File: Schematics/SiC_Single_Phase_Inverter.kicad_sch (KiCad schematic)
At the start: 4 parts, among them J1 23AH8786-Red, J2 23AH8785-Black, J3 23AH8786-Red, J4 23AH8785-Black

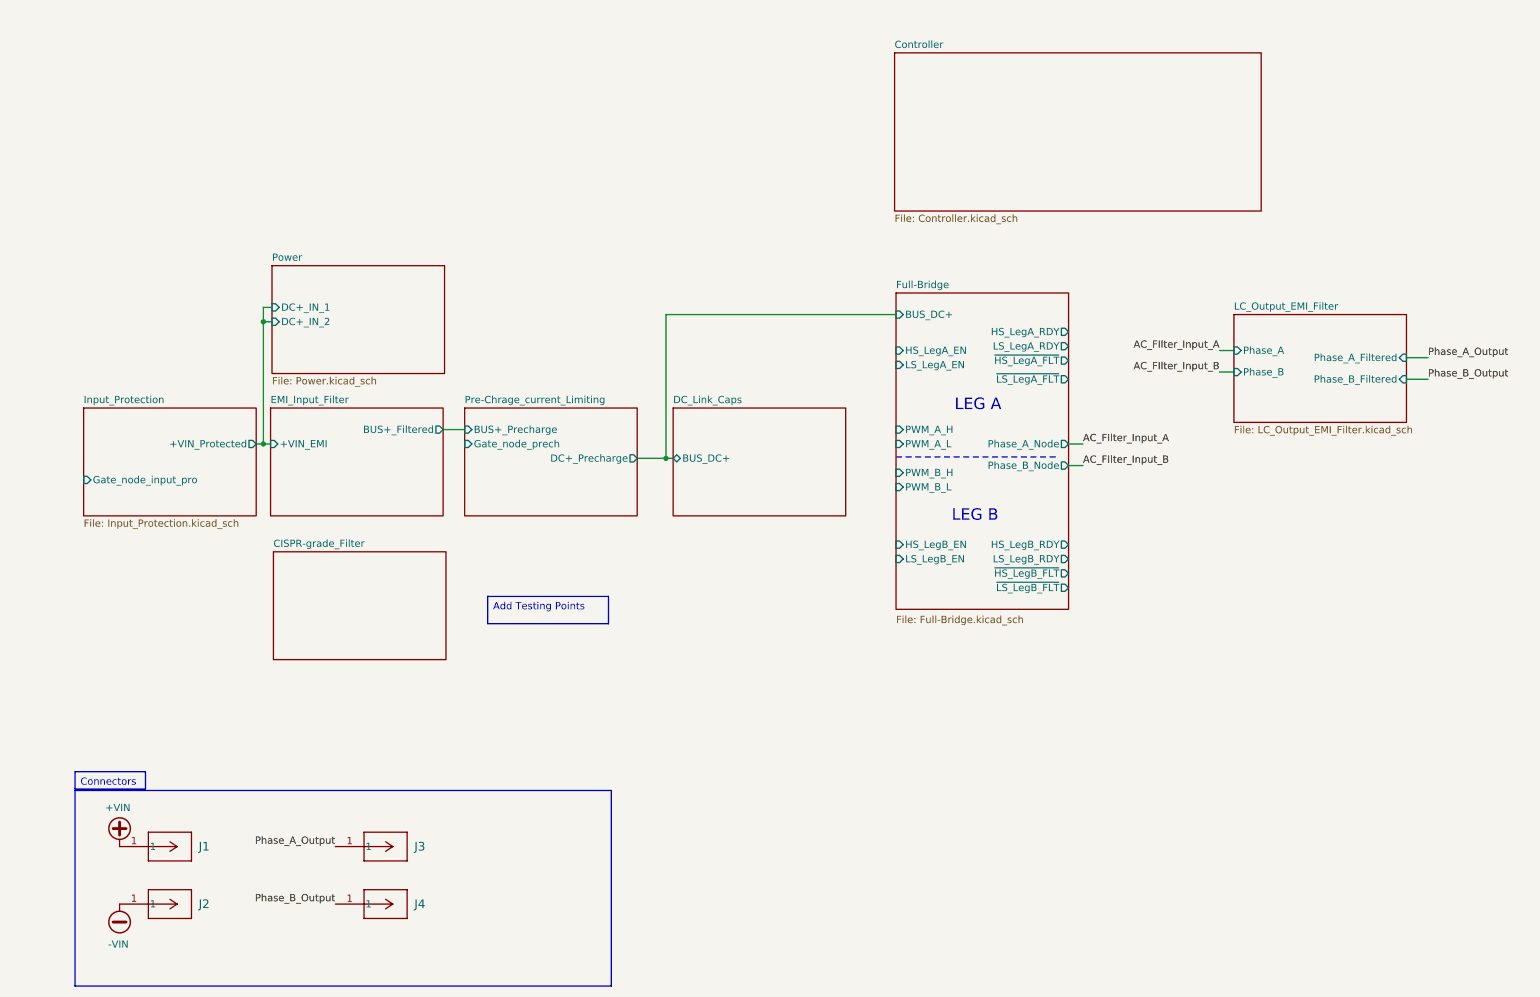
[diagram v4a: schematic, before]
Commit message: WIP: Work on Controller layout, and fixed some sheet text and positions
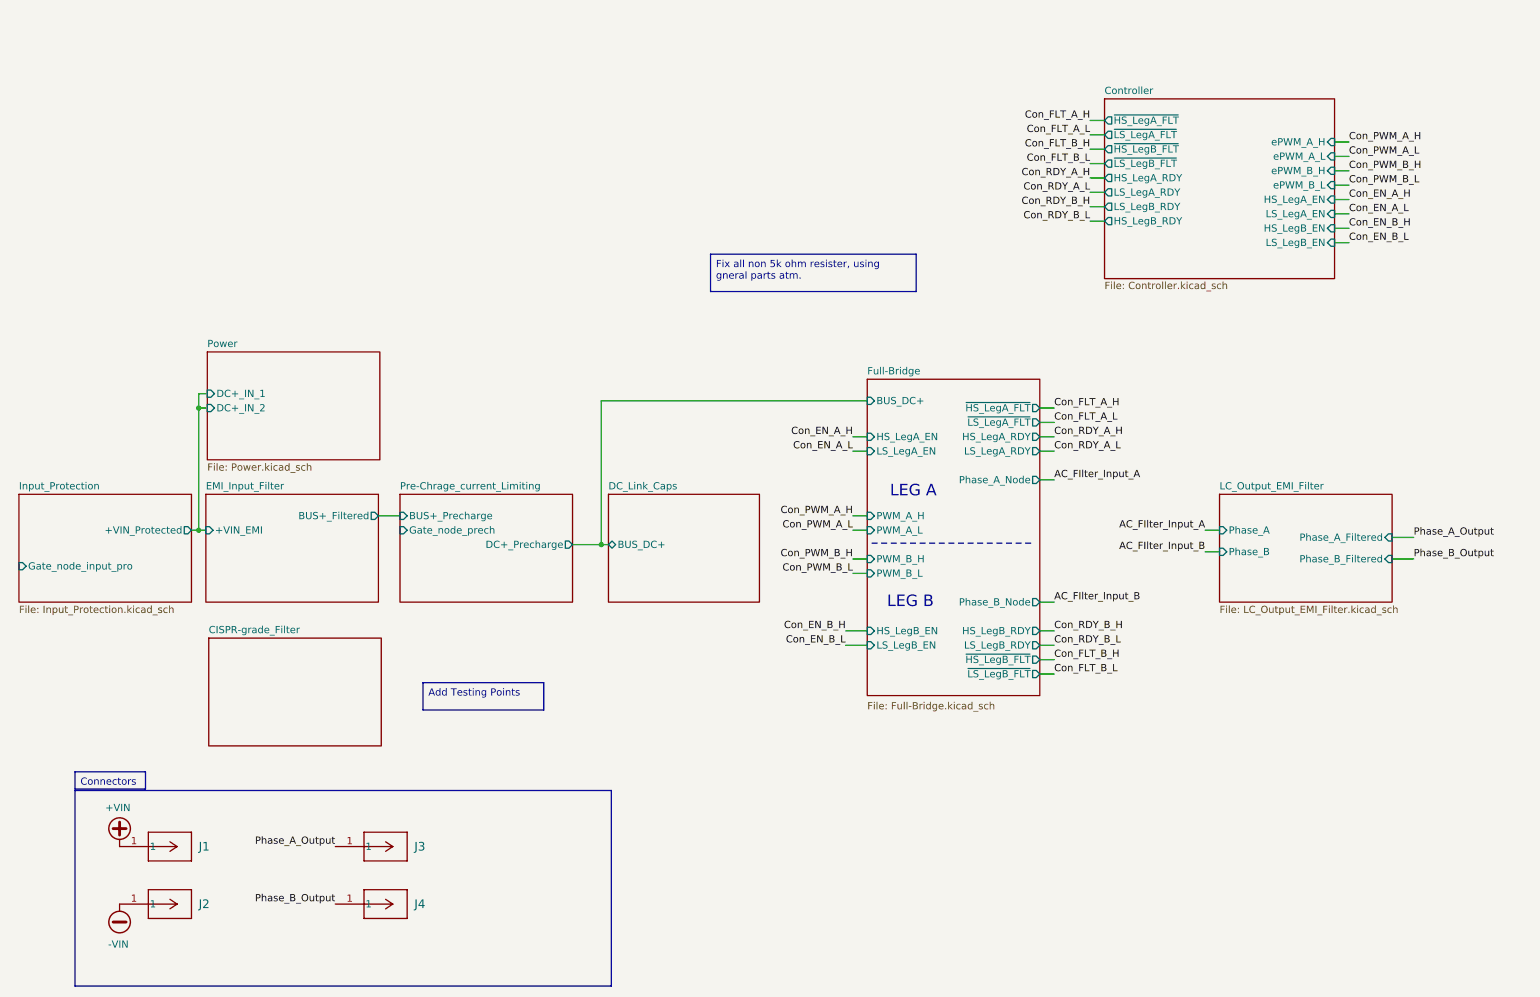
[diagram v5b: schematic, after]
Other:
- sheet Controller ports: added HS_LegA_EN, HS_LegA_RDY, HS_LegB_EN, HS_LegB_RDY, LS_LegA_EN, LS_LegA_RDY, LS_LegB_EN, LS_LegB_RDY, ePWM_A_H, ePWM_A_L, ePWM_B_H, ePWM_B_L, ~{HS_LegA_FLT}, ~{HS_LegB_FLT}, ~{LS_LegA_FLT}, ~{LS_LegB_FLT}; removed none

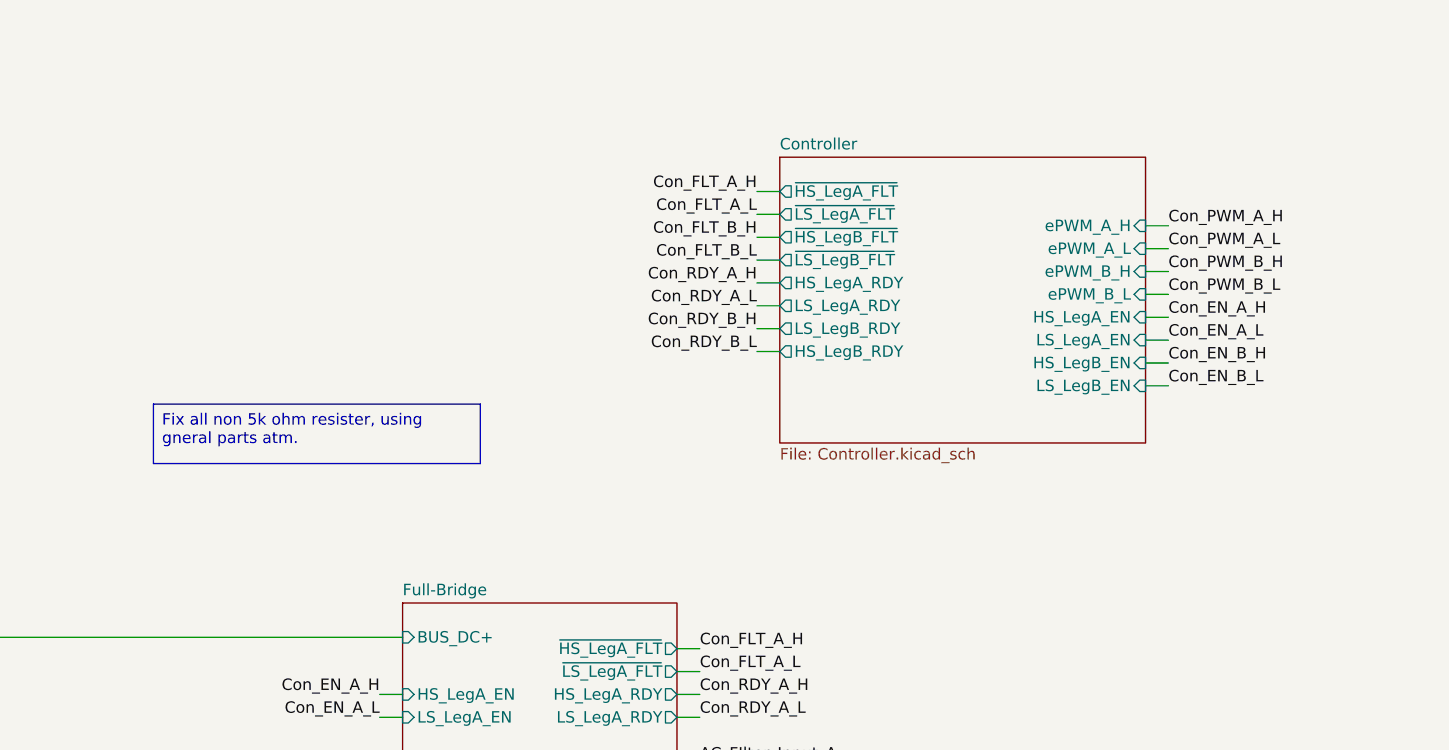
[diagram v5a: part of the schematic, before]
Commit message: [WIP Controller Subsheet]
- Added USB sub sheet to allow use of a USB connection to controller
- Added USB parts for USB Circuit
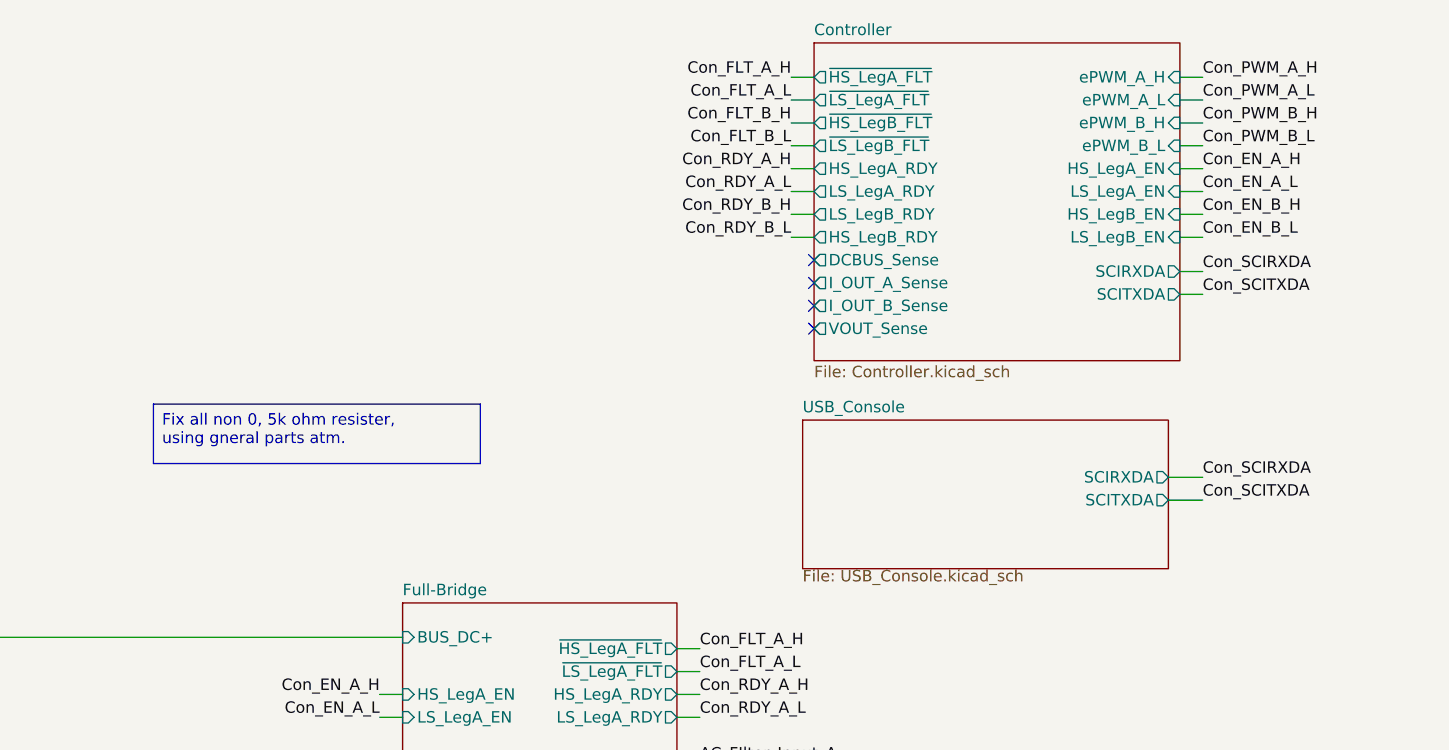
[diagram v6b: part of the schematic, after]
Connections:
- no-connect marks 0 -> 4
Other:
- added sheet USB_Console (USB_Console.kicad_sch)
- sheet Controller ports: added DCBUS_Sense, I_OUT_A_Sense, I_OUT_B_Sense, SCIRXDA, SCITXDA, VOUT_Sense; removed none

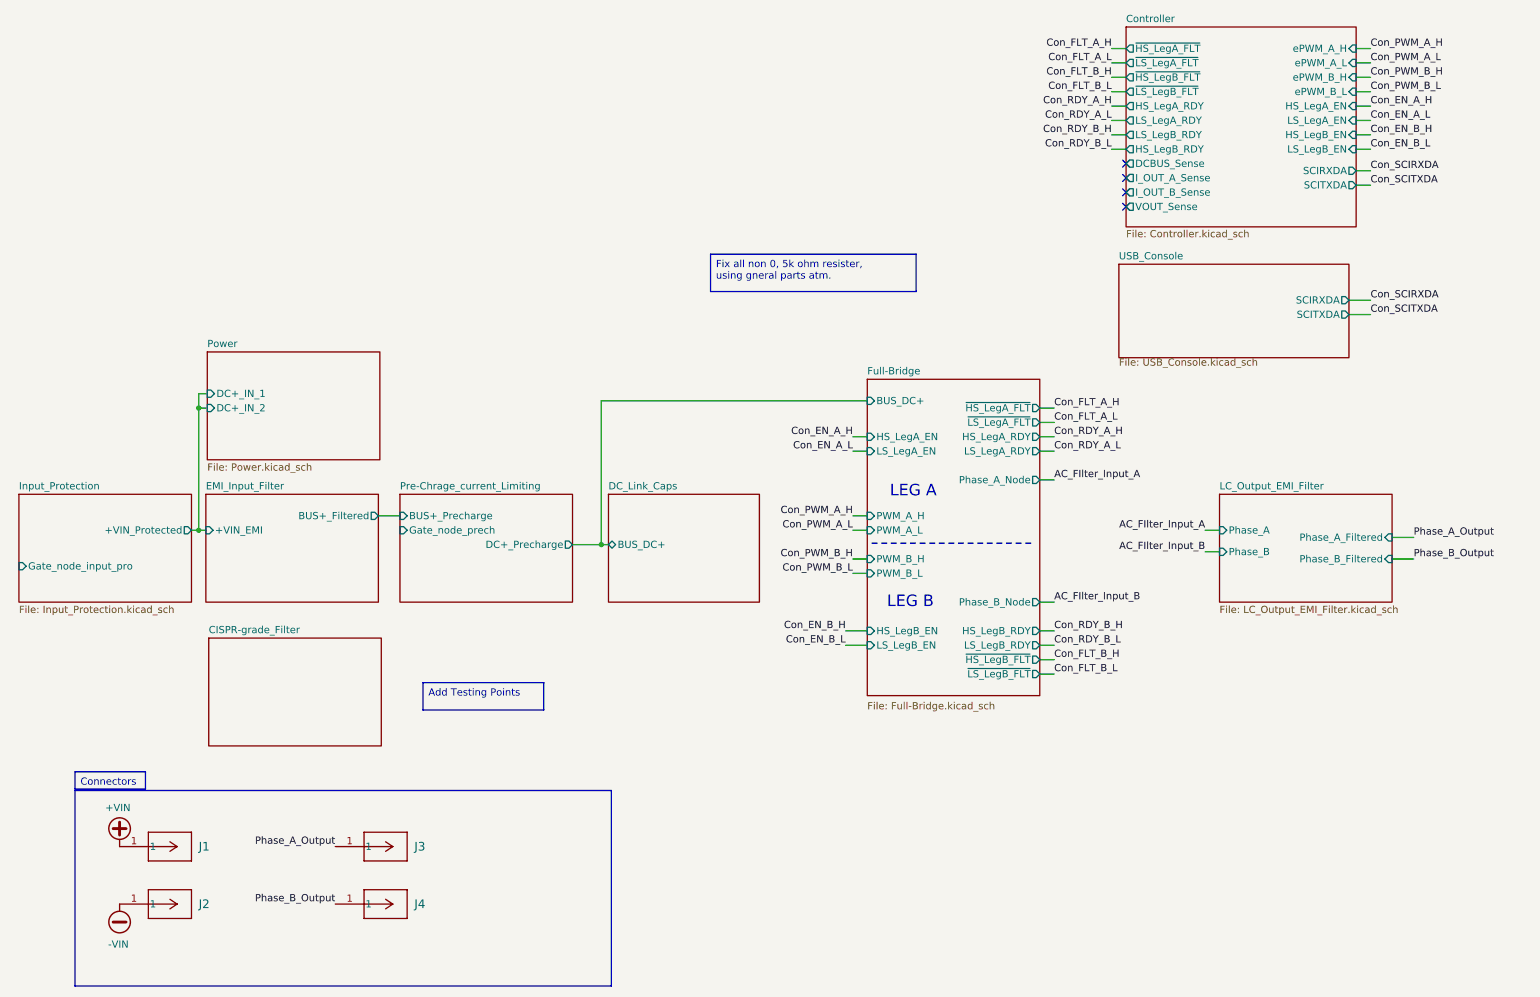
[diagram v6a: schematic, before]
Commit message: [Milestone Compelted Controller and USB]
- Added Test Points
- Completed USB circuit to Controller
- Wired up Controller
- Added Connectors to Power Subsheet and 12pin from cotnroller to Full
  Bridge
- Added 3d models for USB compoents
- General fixes to subsheets
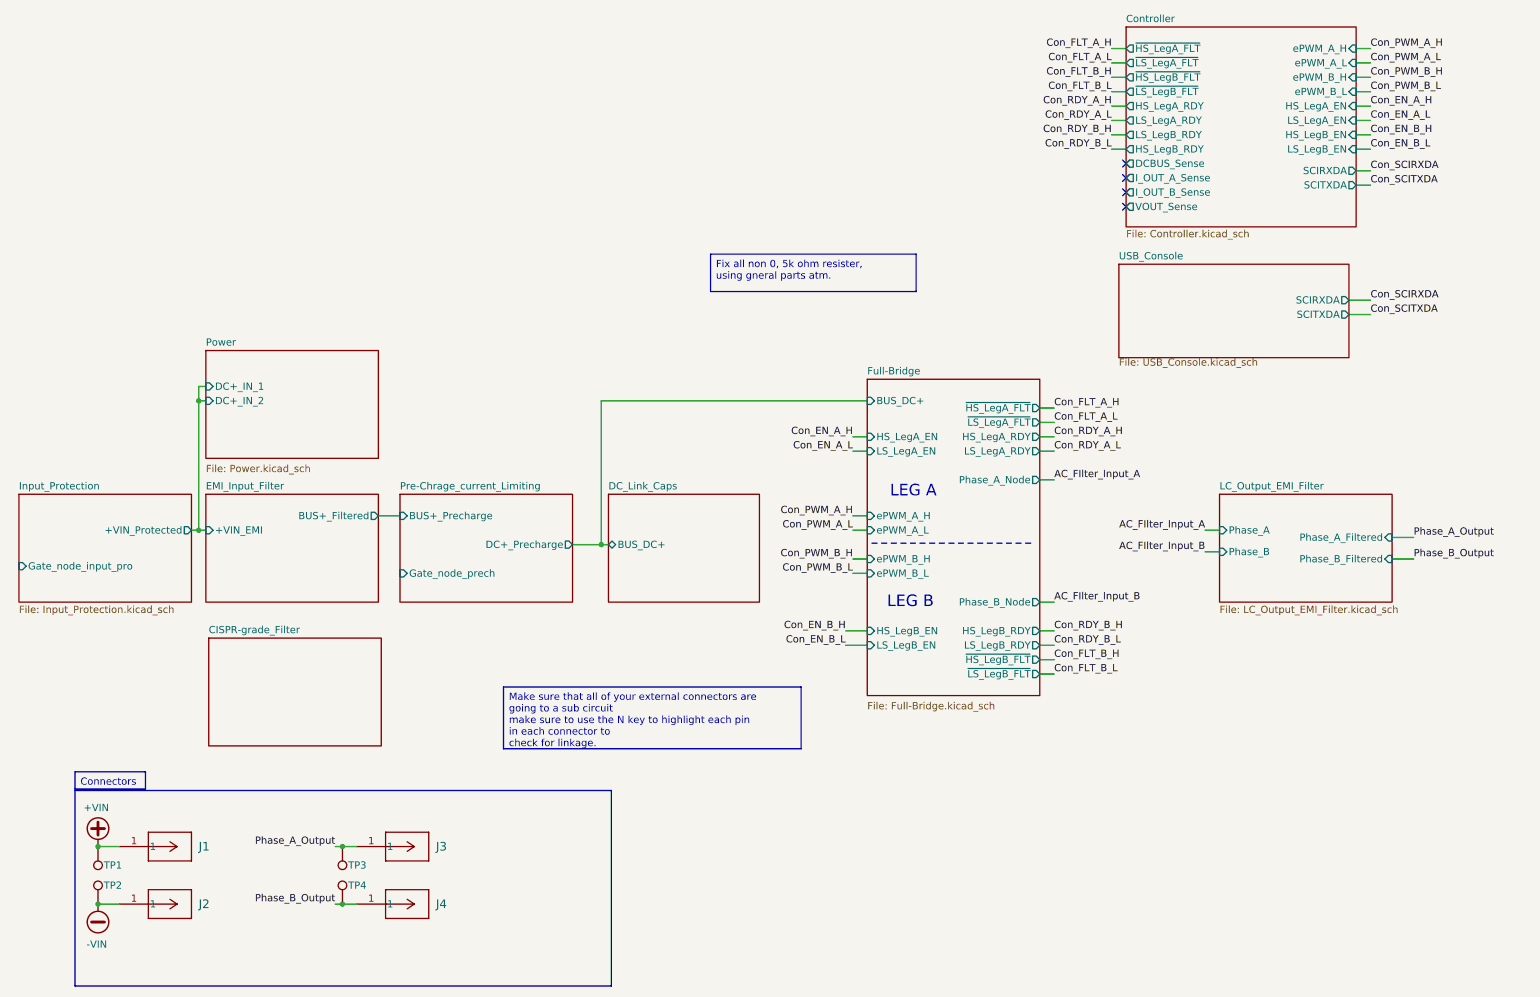
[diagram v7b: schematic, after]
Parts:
- added TP1, TP3: 5277, SiC_Inverter:5277, symbol SiC_Inverter:5277
- added TP2, TP4: 5281, SiC_Inverter:5281, symbol SiC_Inverter:5281
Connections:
- net +VIN: now also TP1.1
- net -VIN: now also TP2.1
- net Phase_A_Output: now also TP3.1
- net Phase_B_Output: now also TP4.1
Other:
- sheet Full-Bridge ports: added ePWM_A_H, ePWM_A_L, ePWM_B_H, ePWM_B_L; removed PWM_A_H, PWM_A_L, PWM_B_H, PWM_B_L
- moved on the sheet: J3, J4

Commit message: [WIP Input Protection Circuit to Controller]
- Added Gate node input protection pin to controller
- Added optocoupler to input protection circuit
- Added 3d model for PC817.....
- Updated PCB to test out PCB modularity
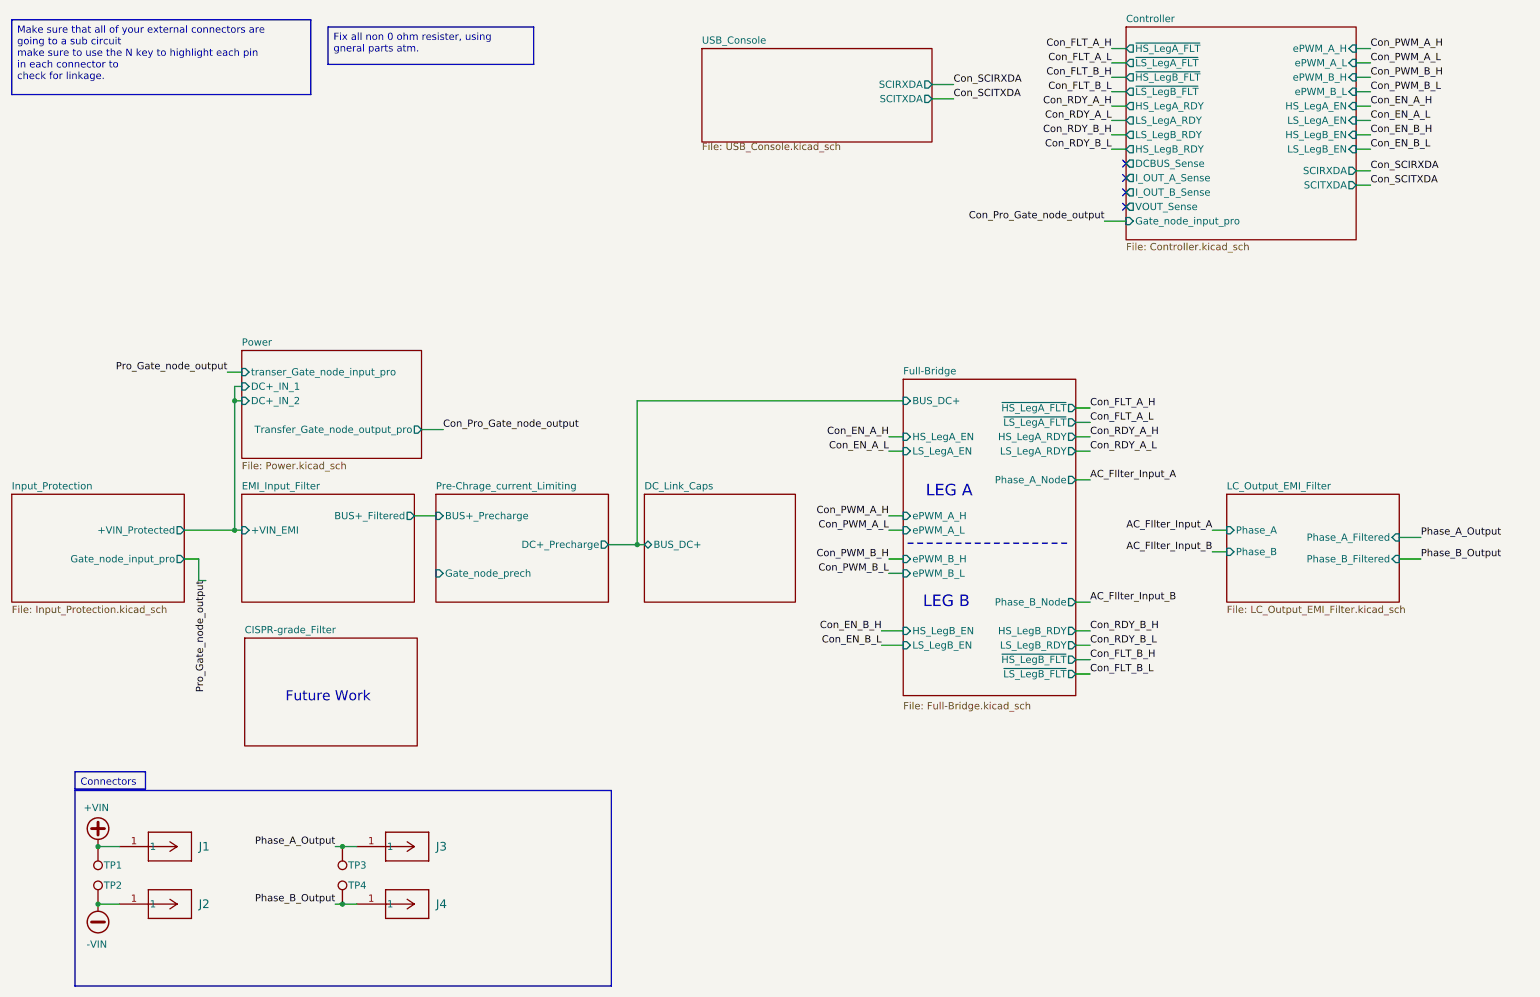
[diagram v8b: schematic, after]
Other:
- sheet Controller ports: added Gate_node_input_pro; removed none
- sheet Power ports: added Transfer_Gate_node_output_pro, transer_Gate_node_input_pro; removed none
- note added: "Future Work"
